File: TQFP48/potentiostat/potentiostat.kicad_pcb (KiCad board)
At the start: 2 copper layers, 1 part, among them U1 AD5941BCPZ

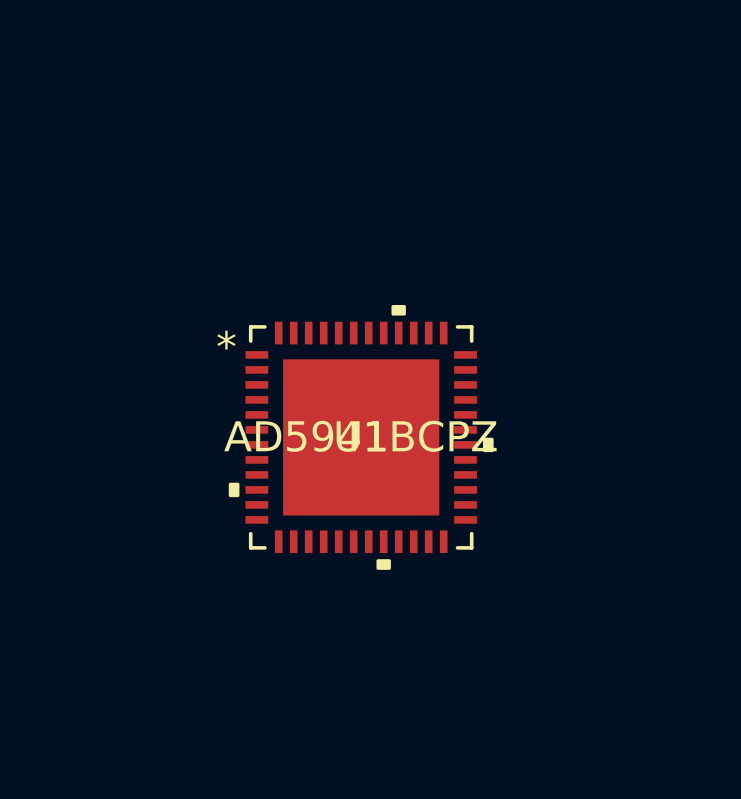
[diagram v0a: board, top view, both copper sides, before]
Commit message: add better connections(3 12pin 1 13 pin generic pin headers)
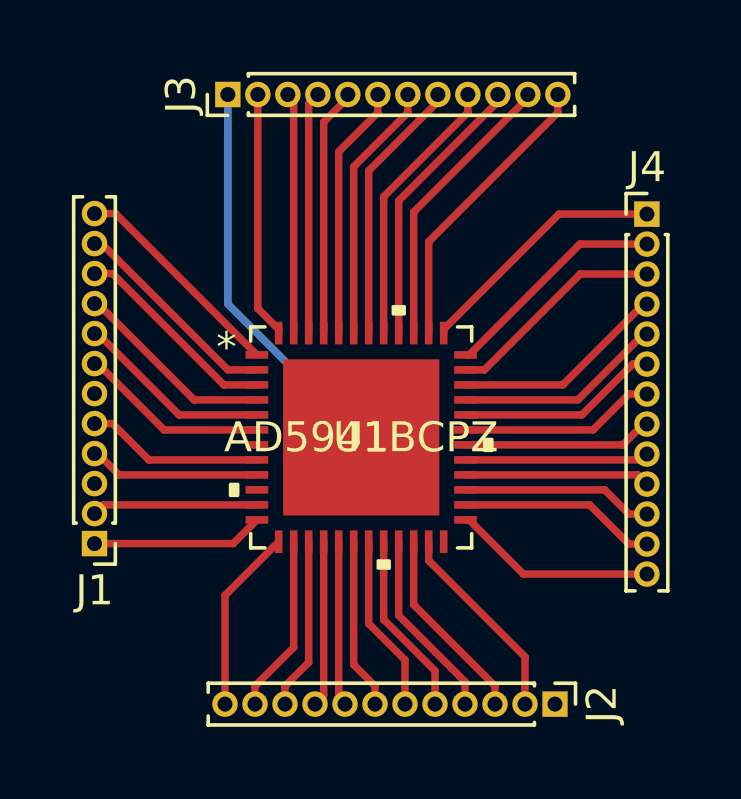
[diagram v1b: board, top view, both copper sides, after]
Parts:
- added J1: Conn_01x12, Connector_PinHeader_1.00mm:PinHeader_1x12_P1.00mm_Vertical, F.Cu at (91.4, 68.3)
- added J2: Conn_01x12, Connector_PinHeader_1.00mm:PinHeader_1x12_P1.00mm_Vertical, F.Cu at (106.8, 73.7)
- added J3: Conn_01x12, Connector_PinHeader_1.00mm:PinHeader_1x12_P1.00mm_Vertical, F.Cu at (95.9, 53.3)
- added J4: Conn_01x13, Connector_PinHeader_1.00mm:PinHeader_1x13_P1.00mm_Vertical, F.Cu at (109.9, 57.3)
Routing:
- net Net-(J3-Pad1): track 0.00 -> 13.3 mm
- net Net-(J3-Pad12): track 0.00 -> 9.74 mm
- net Net-(J3-Pad11): track 0.00 -> 9.53 mm
- net Net-(J3-Pad10): track 0.00 -> 9.32 mm
- net Net-(J3-Pad9): track 0.00 -> 9.11 mm
- net Net-(J3-Pad8): track 0.00 -> 8.91 mm
- net Net-(J3-Pad7): track 0.00 -> 8.70 mm
- net Net-(J3-Pad6): track 0.00 -> 8.49 mm
- net Net-(J4-Pad1): track 0.00 -> 8.49 mm
- net Net-(J3-Pad5): track 0.00 -> 8.29 mm
- net Net-(J3-Pad2): track 0.00 -> 8.24 mm
- net Net-(J3-Pad4): track 0.00 -> 8.08 mm
- net Net-(J3-Pad3): track 0.00 -> 8.03 mm
- net Net-(J4-Pad2): track 0.00 -> 7.58 mm
- net Net-(J4-Pad3): track 0.00 -> 7.37 mm
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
